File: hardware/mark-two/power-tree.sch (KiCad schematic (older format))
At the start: 0 parts

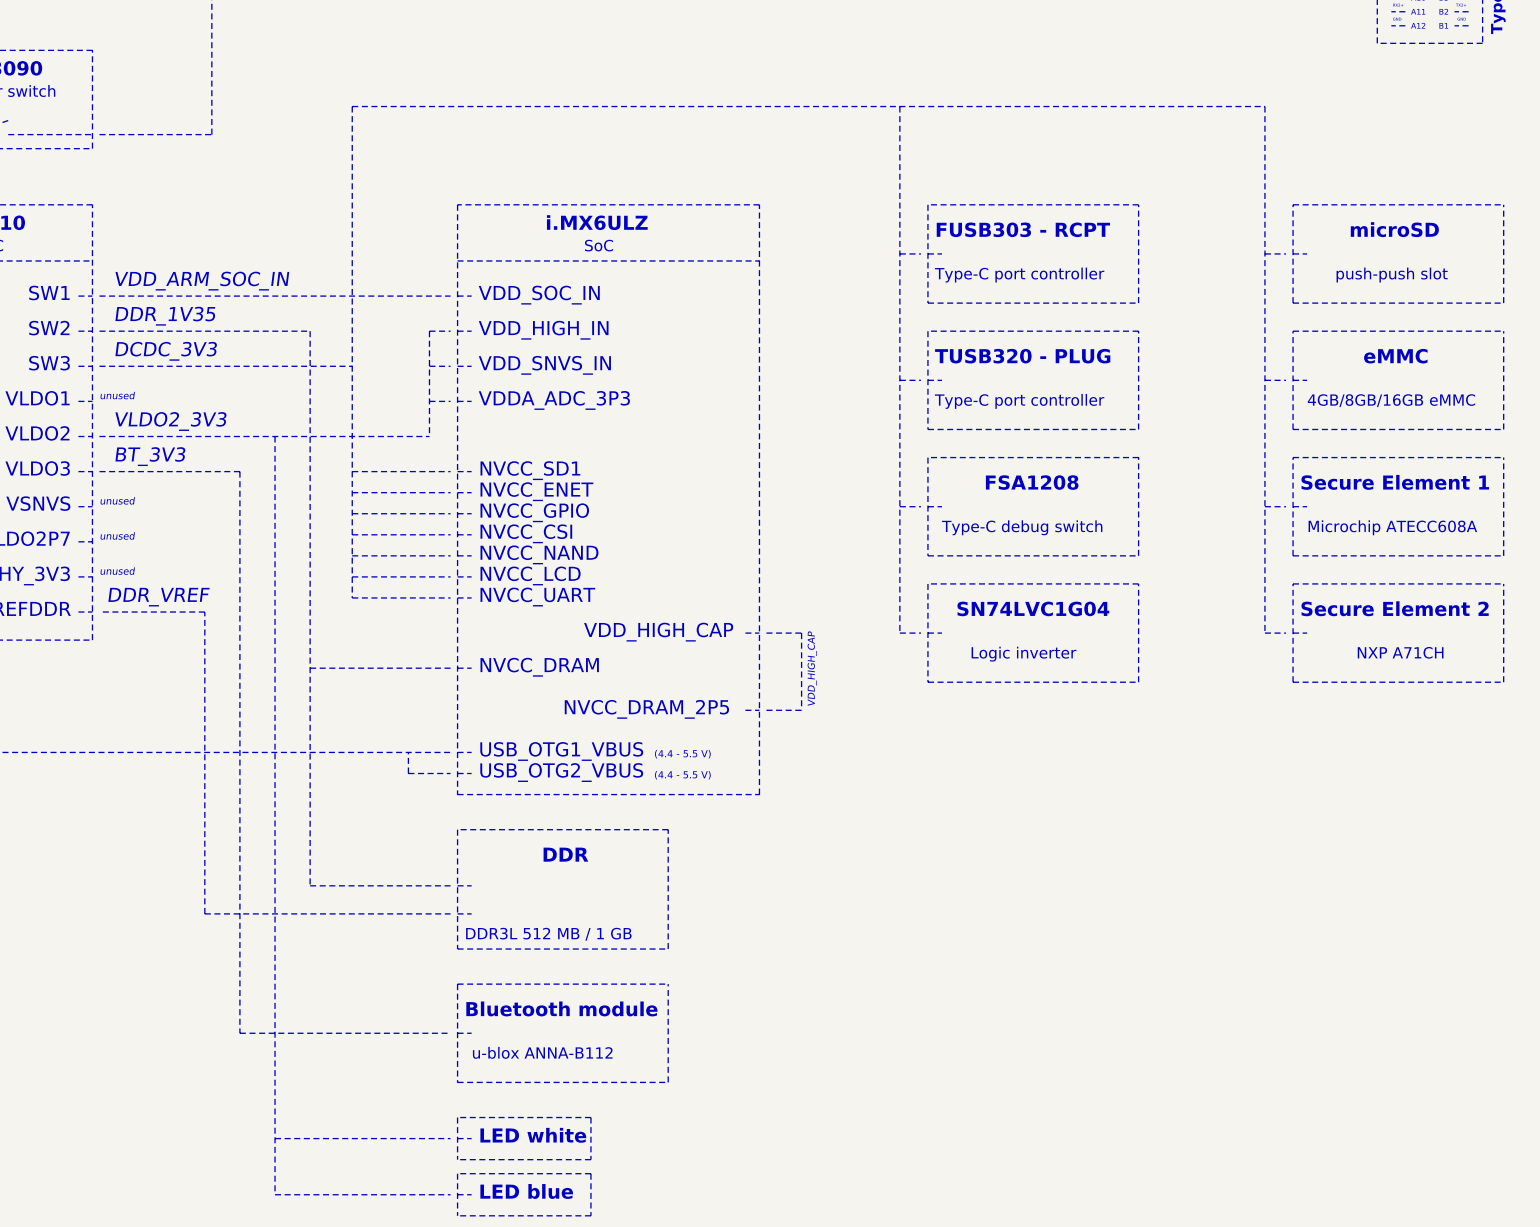
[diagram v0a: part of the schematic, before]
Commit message: add USB armory Mk II rev. γ
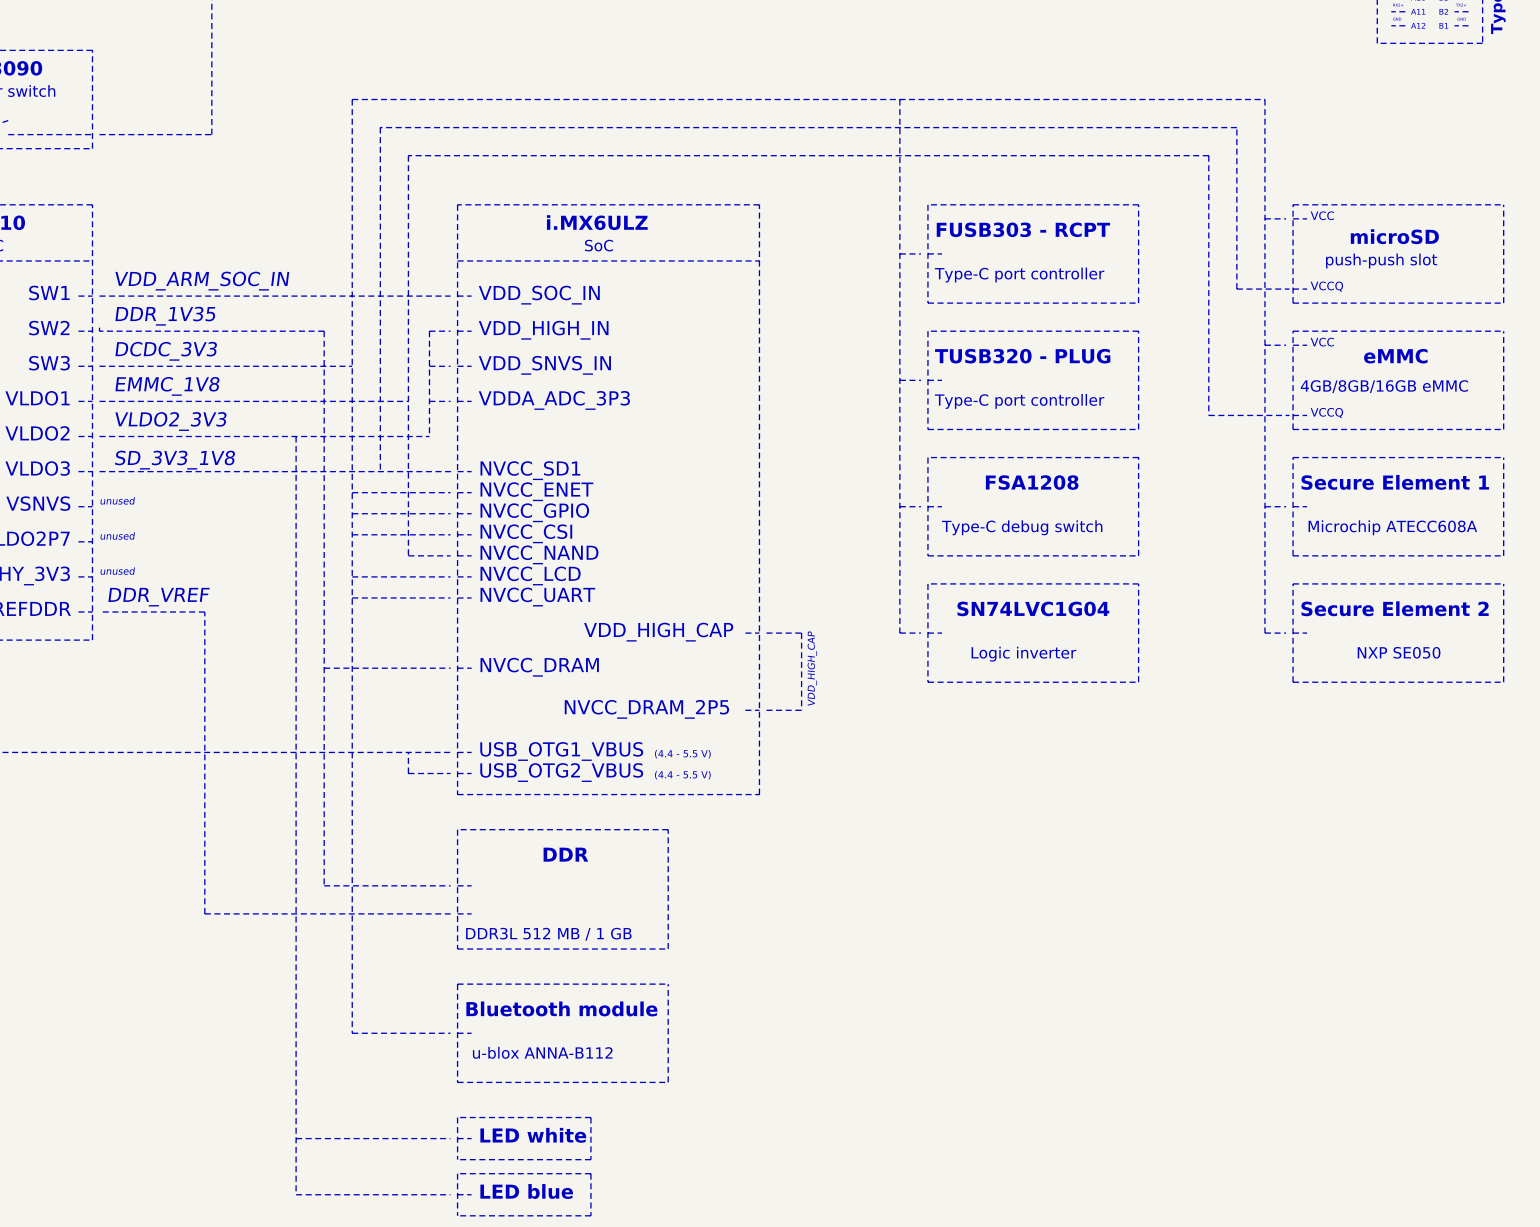
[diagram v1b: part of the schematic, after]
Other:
- note added: "EMMC_1V8"
- note added: "NXP SE050"
- note added: "SD_3V3_1V8"
- note added: "VCC"
- note added: "VCCQ"
- note removed: "BT_3V3"
- note removed: "NXP A71CH"
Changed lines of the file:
@@
 EESchema Schematic File Version 4
-LIBS:armory-cache
 EELAYER 30 0
 EELAYER END
@@
 encoding utf-8
 Sheet 12 13
-Title "USB ARMORY"
-Date "2019-06-25"
-Rev "MARK II"
+Title "USB armory Mk II"
+Date "2021-02-18"
+Rev "γ"
 Comp "F-Secure"
-Comment1 "Copyright © 2019 F-Secure"
-Comment2 "License: CERN OHL v1.2"
-Comment3 "https://github.com/inversepath/usbarmory"
+Comment1 "Copyright © F-Secure Corporation"
+Comment2 "License: CERN-OHL-S"
+Comment3 "https://github.com/f-secure-foundry/usbarmory"
 Comment4 ""
 $EndDescr
@@
 Text Notes 11900 5650 0    100  ~ 20
 FSA1208
-Text Notes 14400 4150 0    80   ~ 0
+Text Notes 14325 4050 0    80   ~ 0
 push-push slot
-Text Notes 14500 3850 0    100  ~ 20
+Text Notes 14500 3900 0    100  ~ 20
 microSD
 Wire Notes Line width 20 style solid rgb(0, 0, 0)
@@
 Wire Notes Line width 20 style solid rgb(0, 0, 0)
 	15600 4300 15600 3600
-Text Notes 14200 5050 0    80   ~ 0
+Text Notes 14150 4950 0    80   ~ 0
 4GB/8GB/16GB eMMC
 Text Notes 14600 4750 0    100  ~ 20
@@
 Wire Notes Line width 20 style solid rgb(194, 0, 194)
 	7950 4500 8100 4500
-Wire Notes Line width 20 style solid rgb(0, 132, 132)
-	7400 5500 8100 5500
 Text Notes 5700 4700 0    100  Italic 0
 DCDC_3V3
-Wire Notes Line width 20 style solid rgb(194, 0, 0)
-	5600 4500 7100 4500
 Text Notes 5700 4450 0    100  Italic 0
 DDR_1V35
-Wire Notes Line width 20 style solid rgb(194, 0, 0)
-	7100 6900 8100 6900
 Wire Notes Line width 20 style solid rgb(194, 0, 194)
 	5600 5250 7950 5250
-Wire Notes Line width 20 style solid rgb(194, 0, 194)
-	7950 4500 7950 5250
 Wire Notes Line width 20 style solid rgb(194, 0, 194)
 	7950 4750 8100 4750
@@
 	7400 5950 8100 5950
 Wire Notes Line width 20 style solid rgb(0, 132, 132)
-	7400 6100 8100 6100
-Wire Notes Line width 20 style solid rgb(0, 132, 132)
 	7400 6250 8100 6250
 Wire Notes Line width 20 style solid rgb(0, 132, 132)
@@
 Wire Notes Line width 20 style solid rgb(194, 0, 0)
 	7800 7650 7800 7500
-Text Notes 5600 5000 0    50   Italic 0
-unused
 Text Notes 5600 6250 0    50   Italic 0
 unused
@@
 unused
 Text Notes 14550 6850 0    80   ~ 0
-NXP A71CH
+NXP SE050
 Text Notes 14150 6550 0    100  ~ 20
 Secure Element 2
@@
 	8150 5000 8250 5000
 Wire Notes Line width 20 style solid rgb(194, 0, 0)
-	7100 4500 7100 8450
-Wire Notes Line width 20 style solid rgb(194, 0, 0)
-	7100 8450 8100 8450
-Wire Notes Line width 20 style solid
-	5600 5500 6600 5500
-Wire Notes Line width 20 style solid
-	6600 5500 6600 9500
-Wire Notes Line width 20 style solid
-	6600 9500 8100 9500
-Text Notes 5700 5450 0    100  Italic 0
-BT_3V3
+	7200 4500 7200 8450
 Wire Notes Line width 20 style solid rgb(132, 132, 132)
 	10350 6650 10600 6650
@@
 	8150 3600 8150 7800
 Wire Notes Line width 20 style solid rgb(0, 132, 132)
-	7400 2900 7400 6400
-Wire Notes Line width 20 style solid rgb(0, 132, 132)
-	7400 2900 13900 2900
-Wire Notes Line width 20 style solid rgb(0, 132, 132)
-	13900 2900 13900 6650
+	7400 2850 13900 2850
 Wire Notes Line width 20 style solid rgb(0, 132, 132)
 	13900 6650 14050 6650
@@
 	13900 5750 14050 5750
 Wire Notes Line width 20 style solid rgb(0, 132, 132)
-	13900 4850 14050 4850
-Wire Notes Line width 20 style solid rgb(0, 132, 132)
-	13900 3950 14050 3950
-Wire Notes Line width 20 style solid rgb(0, 132, 132)
-	11300 2900 11300 6650
+	13900 4600 14050 4600
+Wire Notes Line width 20 style solid rgb(0, 132, 132)
+	13900 3700 14050 3700
 Wire Notes Line width 20 style solid rgb(0, 132, 132)
 	11300 6650 11450 6650
@@
 	14100 5750 14200 5750
 Wire Notes Line width 20 style solid rgb(0, 0, 0)
-	14100 4850 14200 4850
-Wire Notes Line width 20 style solid rgb(0, 0, 0)
-	14100 3950 14200 3950
+	14100 4600 14200 4600
 Wire Notes Line width 20 style solid rgb(0, 0, 0)
 	8150 9500 8250 9500
@@
 	9100 10500 9100 10800
 Wire Notes Line width 20 style solid rgb(194, 0, 194)
-	6850 10250 8100 10250
-Wire Notes Line width 20 style solid rgb(194, 0, 194)
-	6850 10650 8100 10650
-Wire Notes Line width 20 style solid rgb(194, 0, 194)
-	6850 5250 6850 10650
+	7000 5250 7000 10650
 Wire Notes Line width 20 style solid rgb(0, 194, 0)
 	5450 4500 5550 4500
@@
 Text Notes 5010 1330 0    40   ~ 0
 D4
+Text Notes 5700 4950 0    100  Italic 0
+EMMC_1V8
+Wire Notes Line width 20 style solid rgb(0, 0, 0)
+	14100 5100 14200 5100
+Text Notes 14225 4625 0    60   ~ 0
+VCC
+Text Notes 14225 5125 0    60   ~ 0
+VCCQ
+Wire Notes Line width 20 style solid rgb(0, 255, 0)
+	13500 3250 13500 5100
+Wire Notes Line width 20 style solid rgb(0, 255, 0)
+	7800 3250 7800 6100
+Wire Notes Line width 20 style solid rgb(0, 132, 132)
+	7400 9500 8100 9500
+Wire Notes Line width 20 style solid rgb(194, 194, 0)
+	5600 5500 8125 5500
+Wire Notes Line width 20 style solid rgb(0, 0, 0)
+	14100 3700 14200 3700
+Text Notes 14225 3725 0    60   ~ 0
+VCC
+Wire Notes Line width 20 style solid rgb(0, 0, 0)
+	14100 4200 14200 4200
+Text Notes 14225 4225 0    60   ~ 0
+VCCQ
+Wire Notes Line width 20 style solid rgb(194, 194, 0)
+	13700 4200 13700 3050
+Wire Notes Line width 20 style solid rgb(194, 194, 0)
+	7600 3050 7600 5500
+Text Notes 5700 5475 0    100  Italic 0
+SD_3V3_1V8
+Wire Notes Line width 20 style solid rgb(0, 132, 132)
+	13900 2850 13900 6650
+Wire Notes Line width 20 style solid rgb(0, 132, 132)
+	11300 2850 11300 6650
+Wire Notes Line width 20 style solid rgb(0, 132, 132)
+	7400 2850 7400 9500
+Wire Notes Line width 20 style solid rgb(0, 255, 0)
+	7800 6100 8100 6100
+Wire Notes Line width 20 style solid rgb(0, 255, 0)
+	5600 5000 7800 5000
+Wire Notes Line width 20 style solid rgb(194, 194, 0)
+	13700 3050 7600 3050
+Wire Notes Line width 20 style solid rgb(194, 194, 0)
+	13700 4200 14075 4200
+Wire Notes Line width 20 style solid rgb(0, 255, 0)
+	13500 5100 14075 5100
+Wire Notes Line width 20 style solid rgb(0, 255, 0)
+	13500 3250 7800 3250
+Wire Notes Line width 20 style solid rgb(194, 0, 194)
+	7000 10250 8100 10250
+Wire Notes Line width 20 style solid rgb(194, 0, 194)
+	7000 10650 8100 10650
+Wire Notes Line width 20 style solid rgb(194, 0, 0)
+	7200 4500 5600 4500
+Wire Notes Line
+	5600 4500 5600 4475
+Wire Notes Line width 20 style solid rgb(194, 0, 0)
+	7200 8450 8100 8450
+Wire Notes Line width 20 style solid rgb(194, 0, 0)
+	7200 6900 8100 6900
+Wire Notes Line width 20 style solid rgb(194, 0, 194)
+	7950 4500 7950 5250
 $EndSCHEMATC
